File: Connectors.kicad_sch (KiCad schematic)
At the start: 4 parts, among them J1 Conn_01x04_Pin, J2 Conn_01x04_Pin, J3 Conn_01x09_Pin, J4 Conn_02x03_Odd_Even

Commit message: Completed symbol-footprint associations.
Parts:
- J1, J2: footprint (none) -> Connector_PinHeader_2.54mm:PinHeader_1x04_P2.54mm_Vertical
- J3: footprint (none) -> Connector_PinHeader_2.54mm:PinHeader_1x09_P2.54mm_Vertical
- J4: footprint (none) -> Connector_PinHeader_2.54mm:PinHeader_2x03_P2.54mm_Vertical
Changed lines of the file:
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@@
 			)
 		)
-		(property "Footprint" ""
+		(property "Footprint" "Connector_PinHeader_2.54mm:PinHeader_1x09_P2.54mm_Vertical"
 			(at 106.68 48.26 0)
 			(effects
@@
 			)
 		)
-		(property "Footprint" ""
+		(property "Footprint" "Connector_PinHeader_2.54mm:PinHeader_1x04_P2.54mm_Vertical"
 			(at 71.12 40.64 0)
 			(effects
@@
 			)
 		)
-		(property "Footprint" ""
+		(property "Footprint" "Connector_PinHeader_2.54mm:PinHeader_1x04_P2.54mm_Vertical"
 			(at 88.9 40.64 0)
 			(effects
@@
 			)
 		)
-		(property "Footprint" ""
+		(property "Footprint" "Connector_PinHeader_2.54mm:PinHeader_2x03_P2.54mm_Vertical"
 			(at 127 40.64 0)
 			(effects

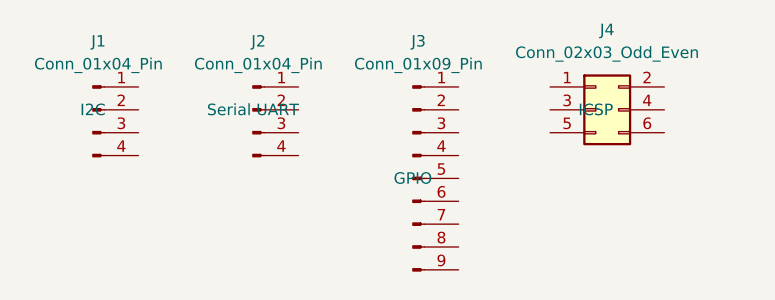
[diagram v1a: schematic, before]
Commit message: Completed wiring in the second sheet.
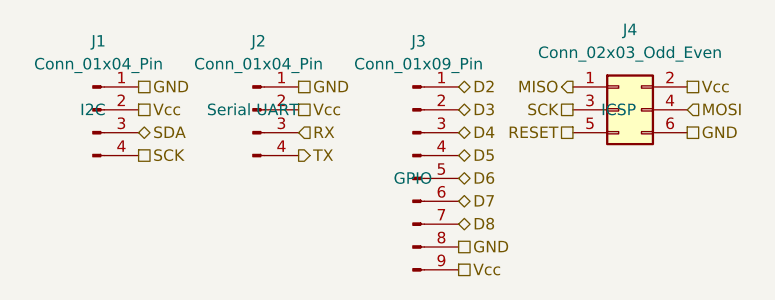
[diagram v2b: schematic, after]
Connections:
- net D2: now reaches J3.1 (Pin_1)
- net D3: now reaches J3.2 (Pin_2)
- net D4: now reaches J3.3 (Pin_3)
- net D5: now reaches J3.4 (Pin_4)
- net D6: now reaches J3.5 (Pin_5)
- net D7: now reaches J3.6 (Pin_6)
- net D8: now reaches J3.7 (Pin_7)
- net GND: now reaches J3.8 (Pin_8)
- net GND: now also J1.1 (Pin_1), J2.1 (Pin_1), J4.6 (Pin_6)
- net Vcc: now reaches J3.9 (Pin_9)
- net Vcc: now also J1.2 (Pin_2), J2.2 (Pin_2), J4.2 (Pin_2)
- net SDA: now reaches J1.3 (Pin_3)
- net SCK: now reaches J1.4 (Pin_4)
- net SCK: now also J4.3 (Pin_3)
- net RX: now reaches J2.3 (Pin_3)
- net TX: now reaches J2.4 (Pin_4)
- net MISO: now reaches J4.1 (Pin_1)
- net MOSI: now reaches J4.4 (Pin_4)
- net RESET: now reaches J4.5 (Pin_5)
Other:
- moved on the sheet: J4

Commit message: Completed comments.
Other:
- moved on the sheet: J1, J2, J3, J4
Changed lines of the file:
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@@
 	(hierarchical_label "RX"
 		(shape input)
-		(at 93.98 43.18 0)
+		(at 134.62 96.52 0)
 		(effects
 			(font
@@
 	(hierarchical_label "D7"
 		(shape bidirectional)
-		(at 111.76 50.8 0)
+		(at 160.02 104.14 0)
 		(effects
 			(font
@@
 	(hierarchical_label "D2"
 		(shape bidirectional)
-		(at 111.76 38.1 0)
+		(at 160.02 91.44 0)
 		(effects
 			(font
@@
 	(hierarchical_label "RESET"
 		(shape passive)
-		(at 124.46 43.18 180)
+		(at 180.34 96.52 180)
 		(effects
 			(font
@@
 	(hierarchical_label "Vcc"
 		(shape passive)
-		(at 93.98 40.64 0)
+		(at 134.62 93.98 0)
 		(effects
 			(font
@@
 	(hierarchical_label "Vcc"
 		(shape passive)
-		(at 137.16 38.1 0)
+		(at 193.04 91.44 0)
 		(effects
 			(font
@@
 	(hierarchical_label "MOSI"
 		(shape input)
-		(at 137.16 40.64 0)
+		(at 193.04 93.98 0)
 		(effects
 			(font
@@
 	(hierarchical_label "D5"
 		(shape bidirectional)
-		(at 111.76 45.72 0)
+		(at 160.02 99.06 0)
 		(effects
 			(font
@@
 	(hierarchical_label "GND"
 		(shape passive)
-		(at 93.98 38.1 0)
+		(at 134.62 91.44 0)
 		(effects
 			(font
@@
 	(hierarchical_label "TX"
 		(shape output)
-		(at 93.98 45.72 0)
+		(at 134.62 99.06 0)
 		(effects
 			(font
@@
 	(hierarchical_label "D4"
 		(shape bidirectional)
-		(at 111.76 43.18 0)
+		(at 160.02 96.52 0)
 		(effects
 			(font
@@
 	(hierarchical_label "MISO"
 		(shape output)
-		(at 124.46 38.1 180)
+		(at 180.34 91.44 180)
 		(effects
 			(font
@@
 	(hierarchical_label "Vcc"
 		(shape passive)
-		(at 76.2 40.64 0)
+		(at 109.22 93.98 0)
 		(effects
 			(font
@@
 	(hierarchical_label "D8"
 		(shape bidirectional)
-		(at 111.76 53.34 0)
+		(at 160.02 106.68 0)
 		(effects
 			(font
@@
 	(hierarchical_label "GND"
 		(shape passive)
-		(at 137.16 43.18 0)
+		(at 193.04 96.52 0)
 		(effects
 			(font
@@
 	(hierarchical_label "GND"
 		(shape passive)
-		(at 76.2 38.1 0)
+		(at 109.22 91.44 0)
 		(effects
 			(font
@@
 	(hierarchical_label "SCK"
 		(shape passive)
-		(at 124.46 40.64 180)
+		(at 180.34 93.98 180)
 		(effects
 			(font
@@
 	(hierarchical_label "SCK"
 		(shape passive)
-		(at 76.2 45.72 0)
+		(at 109.22 99.06 0)
 		(effects
 			(font
@@
 	(hierarchical_label "GND"
 		(shape passive)
-		(at 111.76 55.88 0)
+		(at 160.02 109.22 0)
 		(effects
 			(font
@@
 	(hierarchical_label "D6"
 		(shape bidirectional)
-		(at 111.76 48.26 0)
+		(at 160.02 101.6 0)
 		(effects
 			(font
@@
 	(hierarchical_label "Vcc"
 		(shape passive)
-		(at 111.76 58.42 0)
+		(at 160.02 111.76 0)
 		(effects
 			(font
@@
 	(hierarchical_label "SDA"
 		(shape bidirectional)
-		(at 76.2 43.18 0)
+		(at 109.22 96.52 0)
 		(effects
 			(font
@@
 	(hierarchical_label "D3"
 		(shape bidirectional)
-		(at 111.76 40.64 0)
+		(at 160.02 93.98 0)
 		(effects
 			(font
@@
 	(symbol
 		(lib_id "Connector:Conn_01x09_Pin")
-		(at 106.68 48.26 0)
+		(at 154.94 101.6 0)
 		(unit 1)
 		(exclude_from_sim no)
@@
 		(on_board yes)
 		(dnp no)
-		(fields_autoplaced yes)
 		(property "Reference" "J3"
-			(at 107.315 33.02 0)
+			(at 155.575 86.36 0)
 			(effects
 				(font
@@
 		)
 		(property "Value" "Conn_01x09_Pin"
-			(at 107.315 35.56 0)
+			(at 155.575 88.9 0)
 			(effects
 				(font
@@
 		)
 		(property "Footprint" "Connector_PinHeader_2.54mm:PinHeader_1x09_P2.54mm_Vertical"
-			(at 106.68 48.26 0)
+			(at 154.94 101.6 0)
 			(effects
 				(font
@@
 		)
 		(property "Datasheet" "~"
-			(at 106.68 48.26 0)
+			(at 154.94 101.6 0)
 			(effects
 				(font
@@
 		)
 		(property "Description" "Generic connector, single row, 01x09, script generated"
-			(at 106.68 48.26 0)
+			(at 154.94 101.6 0)
 			(effects
 				(font
@@
 		)
 		(property "Purpose" "GPIO"
-			(at 106.68 48.26 0)
+			(at 152.4 101.6 0)
 			(effects
 				(font
@@
 	(symbol
 		(lib_id "Connector:Conn_01x04_Pin")
-		(at 71.12 40.64 0)
+		(at 104.14 93.98 0)
 		(unit 1)
 		(exclude_from_sim no)
@@
 		(on_board yes)
 		(dnp no)
-		(fields_autoplaced yes)
 		(property "Reference" "J1"
-			(at 71.755 33.02 0)
+			(at 104.775 86.36 0)
 			(effects
 				(font
@@
 		)
 		(property "Value" "Conn_01x04_Pin"
-			(at 71.755 35.56 0)
+			(at 104.775 88.9 0)
 			(effects
 				(font
@@
 		)
 		(property "Footprint" "Connector_PinHeader_2.54mm:PinHeader_1x04_P2.54mm_Vertical"
-			(at 71.12 40.64 0)
+			(at 104.14 93.98 0)
 			(effects
 				(font
@@
 		)
 		(property "Datasheet" "~"
-			(at 71.12 40.64 0)
+			(at 104.14 93.98 0)
 			(effects
 				(font
@@
 		)
 		(property "Description" "Generic connector, single row, 01x04, script generated"
-			(at 71.12 40.64 0)
+			(at 104.14 93.98 0)
 			(effects
 				(font
@@
 		)
 		(property "Purpose" "I2C"
-			(at 71.12 40.64 0)
+			(at 104.14 101.6 0)
 			(effects
 				(font
@@
 	(symbol
 		(lib_id "Connector:Conn_01x04_Pin")
-		(at 88.9 40.64 0)
+		(at 129.54 93.98 0)
 		(unit 1)
 		(exclude_from_sim no)
@@
 		(on_board yes)
 		(dnp no)
-		(fields_autoplaced yes)
 		(property "Reference" "J2"
-			(at 89.535 33.02 0)
+			(at 130.175 86.36 0)
 			(effects
 				(font
@@
 		)
 		(property "Value" "Conn_01x04_Pin"
-			(at 89.535 35.56 0)
+			(at 130.175 88.9 0)
 			(effects
 				(font
@@
 		)
 		(property "Footprint" "Connector_PinHeader_2.54mm:PinHeader_1x04_P2.54mm_Vertical"
-			(at 88.9 40.64 0)
+			(at 129.54 93.98 0)
 			(effects
 				(font
@@
 		)
 		(property "Datasheet" "~"
-			(at 88.9 40.64 0)
+			(at 129.54 93.98 0)
 			(effects
 				(font
@@
 		)
 		(property "Description" "Generic connector, single row, 01x04, script generated"
-			(at 88.9 40.64 0)
+			(at 129.54 93.98 0)
 			(effects
 				(font
@@
 		)
 		(property "Purpose" "Serial UART"
-			(at 88.9 40.64 0)
+			(at 129.54 101.6 0)
 			(effects
 				(font
@@
 	(symbol
 		(lib_id "Connector_Generic:Conn_02x03_Odd_Even")
-		(at 129.54 40.64 0)
+		(at 185.42 93.98 0)
 		(unit 1)
 		(exclude_from_sim no)
@@
 		(dnp no)
 		(property "Reference" "J4"
-			(at 130.81 31.75 0)
+			(at 186.69 85.09 0)
 			(effects
 				(font
@@
 		)
 		(property "Value" "Conn_02x03_Odd_Even"
-			(at 130.81 34.29 0)
+			(at 186.69 87.63 0)
 			(effects
 				(font
@@
 		)
 		(property "Footprint" "Connector_PinHeader_2.54mm:PinHeader_2x03_P2.54mm_Vertical"
-			(at 129.54 40.64 0)
+			(at 185.42 93.98 0)
 			(effects
 				(font
@@
 		)
 		(property "Datasheet" "~"
-			(at 129.54 40.64 0)
+			(at 185.42 93.98 0)
 			(effects
 				(font
@@
 		)
 		(property "Description" "Generic connector, double row, 02x03, odd/even pin numbering scheme (row 1 odd numbers, row 2 even numbers), script generated (kicad-library-utils/schlib/autogen/connector/)"
-			(at 129.54 40.64 0)
+			(at 185.42 93.98 0)
 			(effects
 				(font
@@
 		)
 		(property "Purpose" "ICSP"
-			(at 129.54 40.64 0)
-			(effects
-				(font
+			(at 185.42 99.06 0)
+			(effects
+				(font

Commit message: Add files via upload
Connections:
- net SCK: no longer J1.4 (Pin_4)
- new net SCL: J1.4 (Pin_4)
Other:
- note added: "Connectors"
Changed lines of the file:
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@@
 	(generator_version "9.0")
 	(paper "A4")
+	(text "Connectors"
+		(exclude_from_sim no)
+		(at 101.6 81.28 0)
+		(effects
+			(font
+				(size 1.27 1.27)
+			)
+		)
+	)
 	(hierarchical_label "RX"
 		(shape input)
@@
 		)
 	)
-	(hierarchical_label "SCK"
+	(hierarchical_label "SCL"
 		(shape passive)
 		(at 109.22 99.06 0)
@@
 		)
 	)
+	(rule_area
+		(polyline
+			(pts
+				(xy 96.52 83.82) (xy 200.66 83.82) (xy 200.66 114.3) (xy 96.52 114.3)
+			)
+			(stroke
+				(width 0)
+				(type dash)
+			)
+			(fill
+				(type none)
+			)
+		)
+	)
